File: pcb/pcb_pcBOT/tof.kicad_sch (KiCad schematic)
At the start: 5 parts, among them U501 VL53L0CXV0DH1

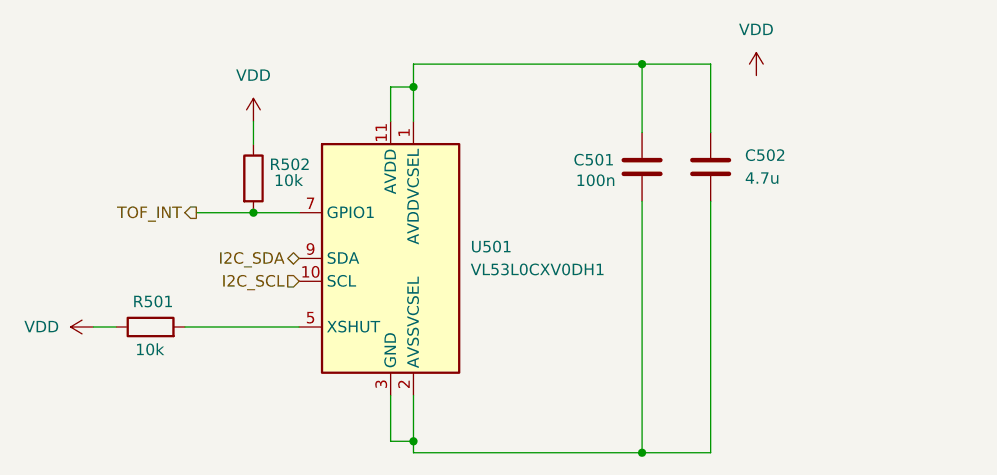
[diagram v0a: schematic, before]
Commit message: Ajout empreintes (incomplet) + test erc correct
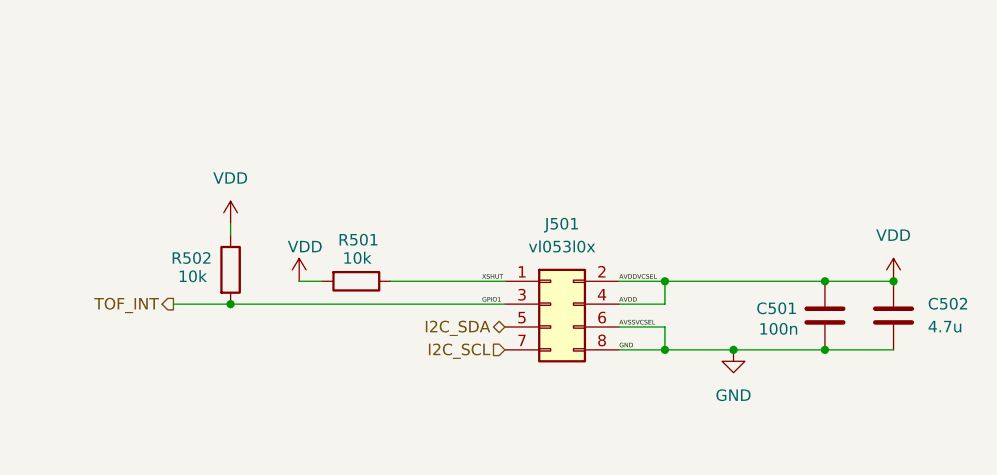
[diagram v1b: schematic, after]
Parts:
- removed U501: VL53L0CXV0DH1, Sensor_Distance:ST_VL53L1x, symbol Sensor_Distance:VL53L0CXV0DH1
- added J501: vl053l0x, symbol Connector_Generic:Conn_02x04_Odd_Even
- C501, C502: footprint (none) -> Capacitor_SMD:C_0805_2012Metric_Pad1.18x1.45mm_HandSolder
- R501, R502: footprint (none) -> Resistor_SMD:R_0805_2012Metric_Pad1.20x1.40mm_HandSolder
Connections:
- net I2C_SCL: now also J501.7 (Pin_7)
- net I2C_SDA: now also J501.5 (Pin_5)
- net TOF_INT: now also J501.3 (Pin_3)
- net VDD: now also C501.1, C502.1, R501.2, J501.2 (Pin_2), J501.4 (Pin_4); no longer R501.1
- net GND: now reaches C501.2, C502.2
- net GND: now also J501.6 (Pin_6), J501.8 (Pin_8)
- new net XSHUT: J501.1 (Pin_1), R501.1
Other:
- moved on the sheet: C501, C502, R501, R502

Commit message: Revert "Ajout empreintes (incomplet) + test erc correct"
This reverts commit 267ed5519d67c336b99c9c80b0ac2067182b82a3.
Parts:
- removed J501: vl053l0x, symbol Connector_Generic:Conn_02x04_Odd_Even
- added U501: VL53L0CXV0DH1, Sensor_Distance:ST_VL53L1x, symbol Sensor_Distance:VL53L0CXV0DH1
- C501, C502: footprint Capacitor_SMD:C_0805_2012Metric_Pad1.18x1.45mm_HandSolder -> (none)
- R501, R502: footprint Resistor_SMD:R_0805_2012Metric_Pad1.20x1.40mm_HandSolder -> (none)
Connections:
- net XSHUT is gone; now on net VDD: R501.1
- net I2C_SCL: now also U501.10 (SCL)
- net I2C_SDA: now also U501.9 (SDA)
- net TOF_INT: now also U501.7 (GPIO1)
- net VDD: no longer C501.1, C502.1, R501.2
- net GND: no longer names the net of C501.2, C502.2
- net GND: now also U501.12 (GND), U501.2 (AVSSVCSEL), U501.3 (GND), U501.4 (GND), U501.6 (GND)
- new net: C501.1, C502.1, U501.1 (AVDDVCSEL), U501.11 (AVDD)
- new net: R501.2, U501.5 (XSHUT)
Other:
- moved on the sheet: C501, C502, R501, R502
